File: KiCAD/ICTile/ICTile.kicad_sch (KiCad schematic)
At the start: 12 parts, among them J1 Conn_02x08_Counter_Clockwise, J2 Conn_02x08_Odd_Even, J3 Conn_02x08_Odd_Even, J4 Conn_02x08_Odd_Even, J5 Conn_02x08_Odd_Even, J6 Conn_02x02_Odd_Even, J7 Conn_02x02_Odd_Even

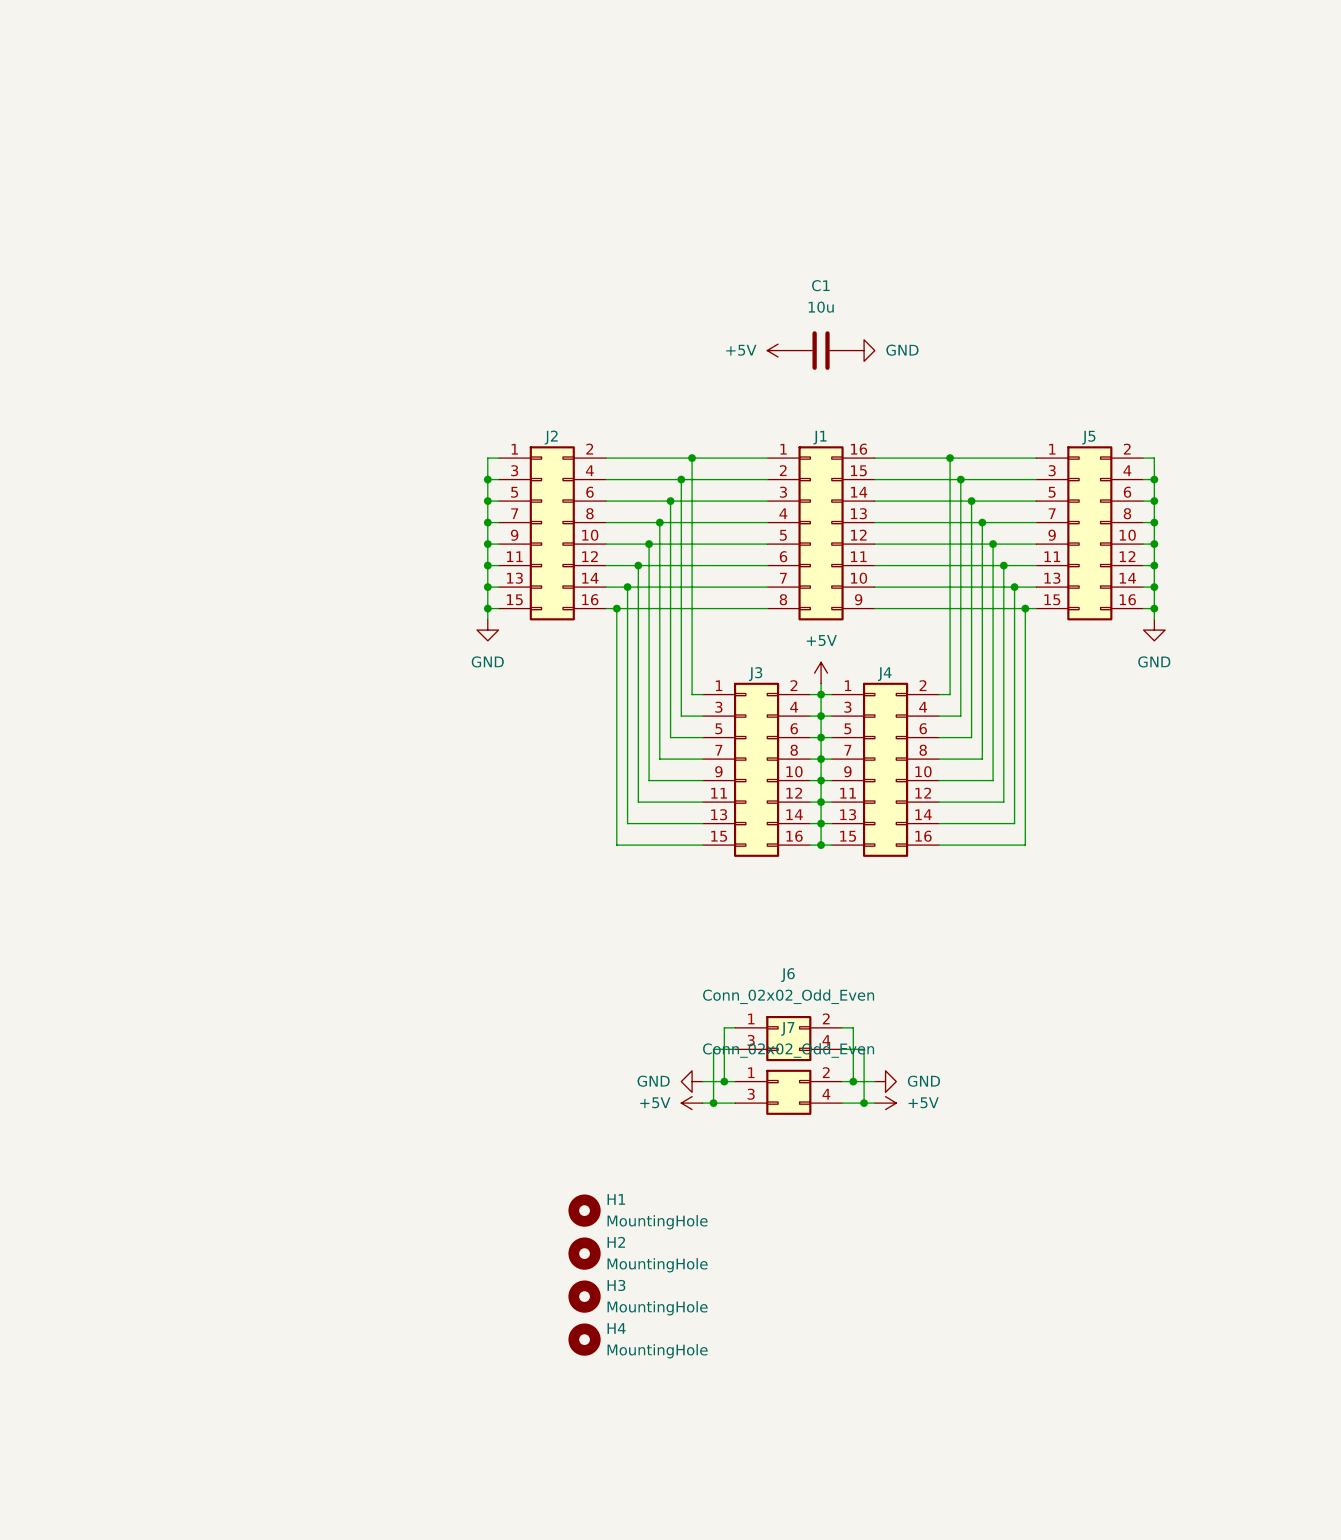
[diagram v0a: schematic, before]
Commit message: Redesign to use 0 Ohm Resistor Jumpers instead of Pin Header Jumpers
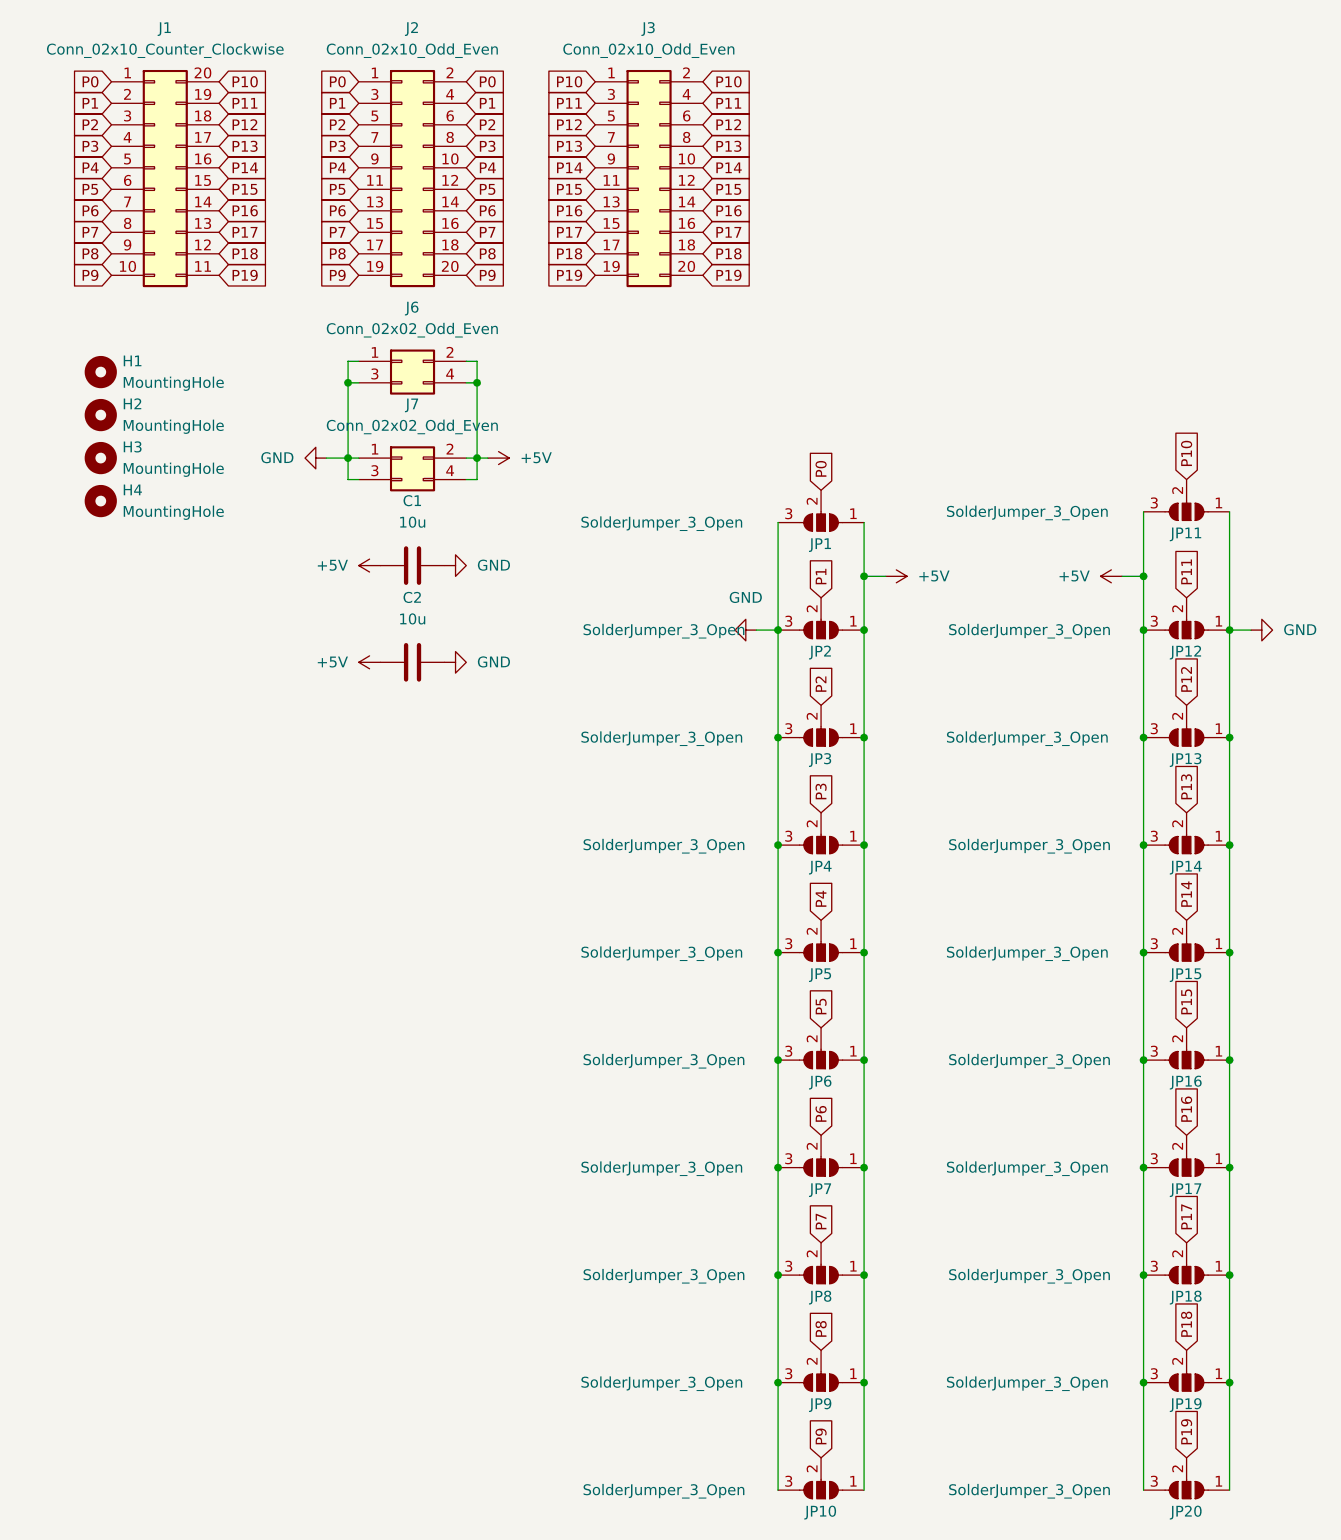
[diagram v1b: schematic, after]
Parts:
- removed J1: Conn_02x08_Counter_Clockwise, Package_DIP:SMDIP-16_W7.62mm, symbol Connector_Generic:Conn_02x08_Counter_Clockwise
- removed J2, J3, J4, J5: Conn_02x08_Odd_Even, Connector_PinHeader_2.54mm:PinHeader_2x08_P2.54mm_Vertical_SMD, symbol Connector_Generic:Conn_02x08_Odd_Even
- added C2: 10u, Capacitor_SMD:C_1206_3216Metric_Pad1.33x1.80mm_HandSolder, symbol Device:C
- added J1: Conn_02x10_Counter_Clockwise, Package_DIP:DIP-20_W8.89mm_SMDSocket_LongPads, symbol Connector_Generic:Conn_02x10_Counter_Clockwise
- added J2, J3: Conn_02x10_Odd_Even, Connector_PinHeader_2.54mm:PinHeader_2x10_P2.54mm_Vertical_SMD, symbol Connector_Generic:Conn_02x10_Odd_Even
- added JP1, JP10, JP11, JP12, JP13, JP14, JP15, JP16, JP17, JP18, JP19, JP2, JP20, JP3, JP4, JP5, JP6, JP7, JP8, JP9: SolderJumper_3_Open, Customs:1206_3Way_Open, symbol Jumper:SolderJumper_3_Open
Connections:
- net +5V: now also J6.2 (Pin_2), J7.2 (Pin_2), C2.1, JP1.1 (A), JP10.1 (A), JP11.3 (B), JP12.3 (B), JP13.3 (B), JP14.3 (B), JP15.3 (B), JP16.3 (B), JP17.3 (B), JP18.3 (B), JP19.3 (B), JP2.1 (A), JP20.3 (B), JP3.1 (A), JP4.1 (A), JP5.1 (A), JP6.1 (A), JP7.1 (A), JP8.1 (A), JP9.1 (A); no longer J6.3 (Pin_3), J7.3 (Pin_3)
- net GND: now also J6.3 (Pin_3), J7.3 (Pin_3), C2.2, JP1.3 (B), JP10.3 (B), JP11.1 (A), JP12.1 (A), JP13.1 (A), JP14.1 (A), JP15.1 (A), JP16.1 (A), JP17.1 (A), JP18.1 (A), JP19.1 (A), JP2.3 (B), JP20.1 (A), JP3.3 (B), JP4.3 (B), JP5.3 (B), JP6.3 (B), JP7.3 (B), JP8.3 (B), JP9.3 (B); no longer J6.2 (Pin_2), J7.2 (Pin_2)
- new net P0: J1.1 (Pin_1), J2.1 (Pin_1), J2.2 (Pin_2), JP1.2 (C)
- new net P1: J1.2 (Pin_2), J2.3 (Pin_3), J2.4 (Pin_4), JP2.2 (C)
- new net P10: J1.20 (Pin_20), J3.1 (Pin_1), J3.2 (Pin_2), JP11.2 (C)
- new net P11: J1.19 (Pin_19), J3.3 (Pin_3), J3.4 (Pin_4), JP12.2 (C)
- new net P12: J1.18 (Pin_18), J3.5 (Pin_5), J3.6 (Pin_6), JP13.2 (C)
- new net P13: J1.17 (Pin_17), J3.7 (Pin_7), J3.8 (Pin_8), JP14.2 (C)
- new net P14: J1.16 (Pin_16), J3.10 (Pin_10), J3.9 (Pin_9), JP15.2 (C)
- new net P15: J1.15 (Pin_15), J3.11 (Pin_11), J3.12 (Pin_12), JP16.2 (C)
- new net P16: J1.14 (Pin_14), J3.13 (Pin_13), J3.14 (Pin_14), JP17.2 (C)
- new net P17: J1.13 (Pin_13), J3.15 (Pin_15), J3.16 (Pin_16), JP18.2 (C)
- new net P18: J1.12 (Pin_12), J3.17 (Pin_17), J3.18 (Pin_18), JP19.2 (C)
- new net P19: J1.11 (Pin_11), J3.19 (Pin_19), J3.20 (Pin_20), JP20.2 (C)
- new net P2: J1.3 (Pin_3), J2.5 (Pin_5), J2.6 (Pin_6), JP3.2 (C)
- new net P3: J1.4 (Pin_4), J2.7 (Pin_7), J2.8 (Pin_8), JP4.2 (C)
- new net P4: J1.5 (Pin_5), J2.10 (Pin_10), J2.9 (Pin_9), JP5.2 (C)
- new net P5: J1.6 (Pin_6), J2.11 (Pin_11), J2.12 (Pin_12), JP6.2 (C)
- new net P6: J1.7 (Pin_7), J2.13 (Pin_13), J2.14 (Pin_14), JP7.2 (C)
- new net P7: J1.8 (Pin_8), J2.15 (Pin_15), J2.16 (Pin_16), JP8.2 (C)
- new net P8: J1.9 (Pin_9), J2.17 (Pin_17), J2.18 (Pin_18), JP9.2 (C)
- new net P9: J1.10 (Pin_10), J2.19 (Pin_19), J2.20 (Pin_20), JP10.2 (C)
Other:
- moved on the sheet: C1, H1, H2, H3, H4, J6, J7
